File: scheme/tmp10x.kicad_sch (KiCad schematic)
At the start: 8 parts, among them U6 TMP100, U7 TMP100

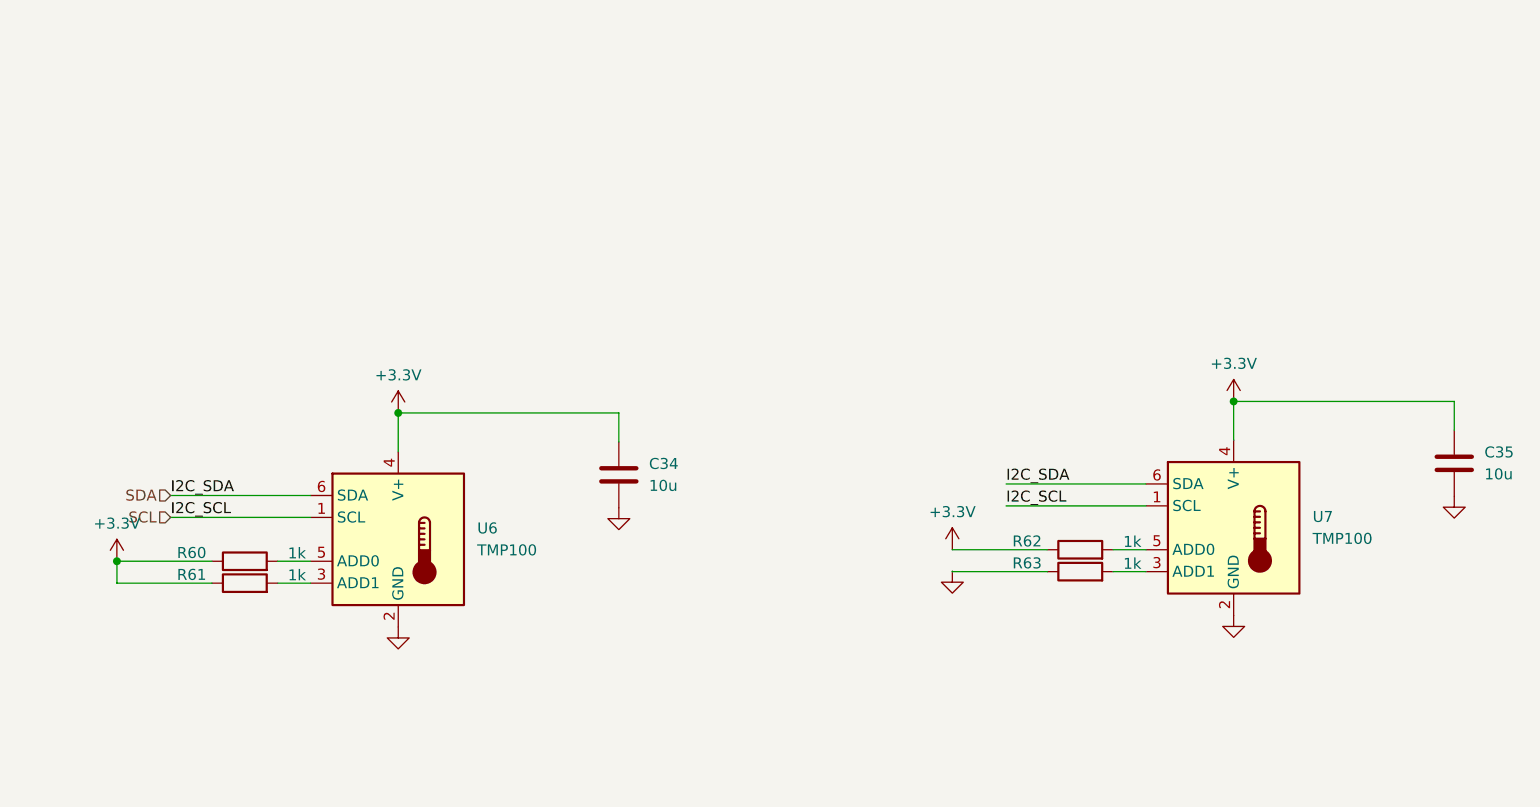
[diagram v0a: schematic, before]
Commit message: feat(schematic): fix peripheral sheets and integrate STM32G0B1CCT6
Главный МК заменён на STM32G0B1CCT6 (LQFP-48, pin-to-pin совместим
с STM32G071CBT6). Лист cpu переписан: обвязка по DS13560, LSE
32.768 кГц, подстроечник на ADC (PA4), перемычка JP_IDD, таблица
назначения выводов.

Исправлены листы периферии:
- st_link: перепутанные USB D+/D-, закороченные резисторы SWD,
  VBUS через PTC и Шоттки, ESD USBLC6-2SC6, LDO AP7361C-33E,
  SWO стянут на землю, J2 1x5 с NRST, перемычка JP_STL_PWR;
- ft232rl: 3V3OUT отвязан от общей шины +3.3V, разделены цепи
  TX/RX и светодиодов, ESD, Шоттки на VBUS, делитель на RESET#;
- w5500: номиналы терминации MDI (49.9 Ом / 10 Ом), PMODE=111,
  RSVD на GND, бусина аналогового питания, подтяжки RST/SCS/INT;
- w32: флэш W25Q32JVSSIQ, символ microSD с детектом карты,
  подтяжки линий SD;
- tmp10x: подтяжки I2C, адреса без резисторов, развязка 100 нФ.

Добавлен лист headers: разъёмы Arduino Uno R3 без ICSP, гребёнки
логического анализатора 1x27 с двух сторон, перемычки JP_SWD.
Удалён пустой лист memory. ERC: 0 ошибок.
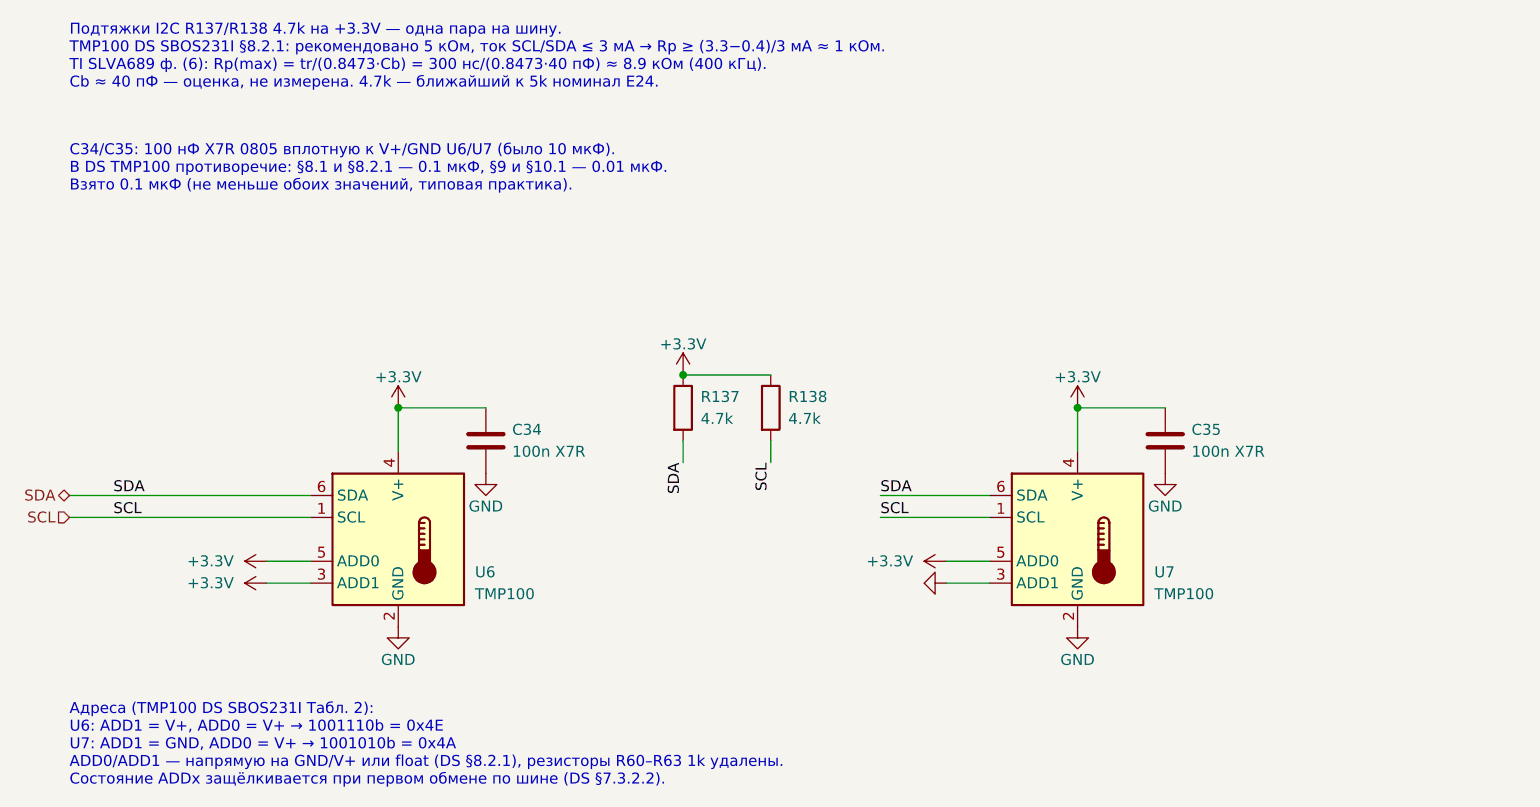
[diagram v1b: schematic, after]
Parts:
- removed R60, R61, R62, R63: 1k, symbol Device:R
- added R137, R138: 4.7k, Resistor_SMD:R_0805_2012Metric, symbol Device:R
- C34, C35: value 10u -> 100n X7R; footprint (none) -> Capacitor_SMD:C_0805_2012Metric
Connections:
- net +3.3V: now also U6.3 (ADD1), U6.5 (ADD0), U7.5 (ADD0), R137.1, R138.1
- net GND: now also U7.3 (ADD1)
- net SCL: now also R138.2
- net SDA: now also R137.2
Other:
- note added: "C34/C35: 100 нФ X7R 0805 вплотную к V+/GND U6/U7 (было 10 мкФ). В DS TMP100 противоречие: §8.1 и §8.2.1 — 0.1 мкФ, §9 и §10.1 — 0.01 мкФ. Взято 0.1 мкФ (не меньше обоих значений, типовая практика)."
- note added: "Адреса (TMP100 DS SBOS231I Табл. 2): U6: ADD1 = V+, ADD0 = V+ → 1001110b = 0x4E U7: ADD1 = GND, ADD0 = V+ → 1001010b = 0x4A ADD0/ADD1 — напрямую на GND/V+ или float (DS §8.2.1), резисторы R60–R63 1k удалены. Состояние ADDx защёлкивается при первом обмене по шине (DS §7.3.2.2)."
- note added: "Подтяжки I2C R137/R138 4.7k на +3.3V — одна пара на шину. TMP100 DS SBOS231I §8.2.1: рекомендовано 5 кОм, ток SCL/SDA ≤ 3 мА → Rp ≥ (3.3−0.4)/3 мА ≈ 1 кОм. TI SLVA689 ф. (6): Rp(max) = tr/(0.8473·Cb) = 300 нс/(0.8473·40 пФ) ≈ 8.9 кОм (400 кГц). Cb ≈ 40 пФ — оценка, не измерена. 4.7k — ближайший к 5k номинал E24."
- moved on the sheet: C34, C35, U7

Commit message: refactor(schematic): re-annotate references by sheet number
Позиционные обозначения перенумерованы по схеме «номер листа x 100»:
cpu - 1xx, st_link - 2xx, ft232rl - 3xx, w5500 - 4xx, w32 - 5xx,
tmp10x - 6xx, leds - 7xx, headers - 8xx. По обозначению на плате
сразу видно, к какому листу относится компонент.

Ссылки на компоненты в текстовых комментариях обновлены. Обозначения
из сторонних референсных схем (MB1136, MB1184, W5500-Ref, Ethernet
Shield, Adafruit) и имена выводов Arduino оставлены без изменений.

Проверено: нетлист до и после совпадает с точностью до переименования
(190 цепей, 187 компонентов), дубликатов нет, ERC - 0 ошибок.
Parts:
- renumbered C34 to C601, C35 to C602, R137 to R601, R138 to R602, U6 to U601, U7 to U602
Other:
- note added: "C601/C602: 100 нФ X7R 0805 вплотную к V+/GND U601/U602 (было 10 мкФ). В DS TMP100 противоречие: §8.1 и §8.2.1 — 0.1 мкФ, §9 и §10.1 — 0.01 мкФ. Взято 0.1 мкФ (не меньше обоих значений, типовая практика)."
- note added: "Адреса (TMP100 DS SBOS231I Табл. 2): U601: ADD1 = V+, ADD0 = V+ → 1001110b = 0x4E U602: ADD1 = GND, ADD0 = V+ → 1001010b = 0x4A ADD0/ADD1 — напрямую на GND/V+ или float (DS §8.2.1), резисторы R60–R63 1k удалены. Состояние ADDx защёлкивается при первом обмене по шине (DS §7.3.2.2)."
- note added: "Подтяжки I2C R601/R602 4.7k на +3.3V — одна пара на шину. TMP100 DS SBOS231I §8.2.1: рекомендовано 5 кОм, ток SCL/SDA ≤ 3 мА → Rp ≥ (3.3−0.4)/3 мА ≈ 1 кОм. TI SLVA689 ф. (6): Rp(max) = tr/(0.8473·Cb) = 300 нс/(0.8473·40 пФ) ≈ 8.9 кОм (400 кГц). Cb ≈ 40 пФ — оценка, не измерена. 4.7k — ближайший к 5k номинал E24."
- note removed: "C34/C35: 100 нФ X7R 0805 вплотную к V+/GND U6/U7 (было 10 мкФ). В DS TMP100 противоречие: §8.1 и §8.2.1 — 0.1 мкФ, §9 и §10.1 — 0.01 мкФ. Взято 0.1 мкФ (не меньше обоих значений, типовая практика)."
- note removed: "Адреса (TMP100 DS SBOS231I Табл. 2): U6: ADD1 = V+, ADD0 = V+ → 1001110b = 0x4E U7: ADD1 = GND, ADD0 = V+ → 1001010b = 0x4A ADD0/ADD1 — напрямую на GND/V+ или float (DS §8.2.1), резисторы R60–R63 1k удалены. Состояние ADDx защёлкивается при первом обмене по шине (DS §7.3.2.2)."
- note removed: "Подтяжки I2C R137/R138 4.7k на +3.3V — одна пара на шину. TMP100 DS SBOS231I §8.2.1: рекомендовано 5 кОм, ток SCL/SDA ≤ 3 мА → Rp ≥ (3.3−0.4)/3 мА ≈ 1 кОм. TI SLVA689 ф. (6): Rp(max) = tr/(0.8473·Cb) = 300 нс/(0.8473·40 пФ) ≈ 8.9 кОм (400 кГц). Cb ≈ 40 пФ — оценка, не измерена. 4.7k — ближайший к 5k номинал E24."
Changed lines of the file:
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@@
 	(generator_version "10.0")
 	(paper "A4")
-	(text "Подтяжки I2C R137/R138 4.7k на +3.3V — одна пара на шину.\nTMP100 DS SBOS231I §8.2.1: рекомендовано 5 кОм, ток SCL/SDA ≤ 3 мА → Rp ≥ (3.3−0.4)/3 мА ≈ 1 кОм.\nTI SLVA689 ф. (6): Rp(max) = tr/(0.8473·Cb) = 300 нс/(0.8473·40 пФ) ≈ 8.9 кОм (400 кГц).\nCb ≈ 40 пФ — оценка, не измерена. 4.7k — ближайший к 5k номинал E24."
+	(text "Подтяжки I2C R601/R602 4.7k на +3.3V — одна пара на шину.\nTMP100 DS SBOS231I §8.2.1: рекомендовано 5 кОм, ток SCL/SDA ≤ 3 мА → Rp ≥ (3.3−0.4)/3 мА ≈ 1 кОм.\nTI SLVA689 ф. (6): Rp(max) = tr/(0.8473·Cb) = 300 нс/(0.8473·40 пФ) ≈ 8.9 кОм (400 кГц).\nCb ≈ 40 пФ — оценка, не измерена. 4.7k — ближайший к 5k номинал E24."
 		(exclude_from_sim no)
 		(at 63.5 30.48 0)
@@
 		)
 	)
-	(text "Адреса (TMP100 DS SBOS231I Табл. 2):\nU6: ADD1 = V+, ADD0 = V+ → 1001110b = 0x4E\nU7: ADD1 = GND, ADD0 = V+ → 1001010b = 0x4A\nADD0/ADD1 — напрямую на GND/V+ или float (DS §8.2.1), резисторы R60–R63 1k удалены.\nСостояние ADDx защёлкивается при первом обмене по шине (DS §7.3.2.2)."
+	(text "Адреса (TMP100 DS SBOS231I Табл. 2):\nU601: ADD1 = V+, ADD0 = V+ → 1001110b = 0x4E\nU602: ADD1 = GND, ADD0 = V+ → 1001010b = 0x4A\nADD0/ADD1 — напрямую на GND/V+ или float (DS §8.2.1), резисторы R60–R63 1k удалены.\nСостояние ADDx защёлкивается при первом обмене по шине (DS §7.3.2.2)."
 		(exclude_from_sim no)
 		(at 63.5 109.22 0)
@@
 		)
 	)
-	(text "C34/C35: 100 нФ X7R 0805 вплотную к V+/GND U6/U7 (было 10 мкФ).\nВ DS TMP100 противоречие: §8.1 и §8.2.1 — 0.1 мкФ, §9 и §10.1 — 0.01 мкФ.\nВзято 0.1 мкФ (не меньше обоих значений, типовая практика)."
+	(text "C601/C602: 100 нФ X7R 0805 вплотную к V+/GND U601/U602 (было 10 мкФ).\nВ DS TMP100 противоречие: §8.1 и §8.2.1 — 0.1 мкФ, §9 и §10.1 — 0.01 мкФ.\nВзято 0.1 мкФ (не меньше обоих значений, типовая практика)."
 		(exclude_from_sim no)
 		(at 63.5 44.45 0)
@@
 		(in_pos_files yes)
 		(dnp no)
-		(property "Reference" "R137"
+		(property "Reference" "R601"
 			(at 136.652 73.66 0)
 			(show_name no)
@@
 			(project "g0_dev_board"
 				(path "/997acf0a-b54e-4c77-ad84-80f8d6e2dc27/1fdcf67e-4ae0-44bf-b3bf-1ed7985b8be2"
-					(reference "R137")
+					(reference "R601")
 					(unit 1)
 				)
@@
 		(in_pos_files yes)
 		(dnp no)
-		(property "Reference" "#PWR088"
+		(property "Reference" "#PWR0117"
 			(at 134.62 74.93 0)
 			(hide yes)
@@
 			(project "g0_dev_board"
 				(path "/997acf0a-b54e-4c77-ad84-80f8d6e2dc27/1fdcf67e-4ae0-44bf-b3bf-1ed7985b8be2"
-					(reference "#PWR088")
+					(reference "#PWR0117")
 					(unit 1)
 				)
@@
 		(in_pos_files yes)
 		(dnp no)
-		(property "Reference" "#PWR087"
+		(property "Reference" "#PWR0119"
 			(at 171.45 95.25 90)
 			(hide yes)
@@
 			(project "g0_dev_board"
 				(path "/997acf0a-b54e-4c77-ad84-80f8d6e2dc27/1fdcf67e-4ae0-44bf-b3bf-1ed7985b8be2"
-					(reference "#PWR087")
+					(reference "#PWR0119")
 					(unit 1)
 				)
@@
 		(in_pos_files yes)
 		(dnp no)
-		(property "Reference" "C35"
+		(property "Reference" "C602"
 			(at 193.548 77.47 0)
 			(show_name no)
@@
 			(project "g0_dev_board"
 				(path "/997acf0a-b54e-4c77-ad84-80f8d6e2dc27/1fdcf67e-4ae0-44bf-b3bf-1ed7985b8be2"
-					(reference "C35")
+					(reference "C602")
 					(unit 1)
 				)
@@
 		(in_pos_files yes)
 		(dnp no)
-		(property "Reference" "#PWR083"
+		(property "Reference" "#PWR0115"
 			(at 101.6 106.68 0)
 			(hide yes)
@@
 			(project "g0_dev_board"
 				(path "/997acf0a-b54e-4c77-ad84-80f8d6e2dc27/1fdcf67e-4ae0-44bf-b3bf-1ed7985b8be2"
-					(reference "#PWR083")
+					(reference "#PWR0115")
 					(unit 1)
 				)
@@
 		(in_pos_files yes)
 		(dnp no)
-		(property "Reference" "U7"
+		(property "Reference" "U602"
 			(at 189.23 93.98 0)
 			(show_name no)
@@
 			(project "g0_dev_board"
 				(path "/997acf0a-b54e-4c77-ad84-80f8d6e2dc27/1fdcf67e-4ae0-44bf-b3bf-1ed7985b8be2"
-					(reference "U7")
+					(reference "U602")
 					(unit 1)
 				)
@@
 		(in_pos_files yes)
 		(dnp no)
-		(property "Reference" "#PWR1305"
+		(property "Reference" "#PWR0118"
 			(at 168.91 92.71 90)
 			(hide yes)
@@
 			(project "g0_dev_board"
 				(path "/997acf0a-b54e-4c77-ad84-80f8d6e2dc27/1fdcf67e-4ae0-44bf-b3bf-1ed7985b8be2"
-					(reference "#PWR1305")
+					(reference "#PWR0118")
 					(unit 1)
 				)
@@
 		(in_pos_files yes)
 		(dnp no)
-		(property "Reference" "U6"
+		(property "Reference" "U601"
 			(at 110.49 93.98 0)
 			(show_name no)
@@
 			(project "g0_dev_board"
 				(path "/997acf0a-b54e-4c77-ad84-80f8d6e2dc27/1fdcf67e-4ae0-44bf-b3bf-1ed7985b8be2"
-					(reference "U6")
+					(reference "U601")
 					(unit 1)
 				)
@@
 		(in_pos_files yes)
 		(dnp no)
-		(property "Reference" "C34"
+		(property "Reference" "C601"
 			(at 114.808 77.47 0)
 			(show_name no)
@@
 			(project "g0_dev_board"
 				(path "/997acf0a-b54e-4c77-ad84-80f8d6e2dc27/1fdcf67e-4ae0-44bf-b3bf-1ed7985b8be2"
-					(reference "C34")
+					(reference "C601")
 					(unit 1)
 				)
@@
 		(in_pos_files yes)
 		(dnp no)
-		(property "Reference" "#PWR1306"
+		(property "Reference" "#PWR0120"
 			(at 180.34 78.74 0)
 			(hide yes)
@@
 			(project "g0_dev_board"
 				(path "/997acf0a-b54e-4c77-ad84-80f8d6e2dc27/1fdcf67e-4ae0-44bf-b3bf-1ed7985b8be2"
-					(reference "#PWR1306")
+					(reference "#PWR0120")
 					(unit 1)
 				)
@@
 		(in_pos_files yes)
 		(dnp no)
-		(property "Reference" "#PWR085"
+		(property "Reference" "#PWR0113"
 			(at 90.17 95.25 90)
 			(hide yes)
@@
 			(project "g0_dev_board"
 				(path "/997acf0a-b54e-4c77-ad84-80f8d6e2dc27/1fdcf67e-4ae0-44bf-b3bf-1ed7985b8be2"
-					(reference "#PWR085")
+					(reference "#PWR0113")
 					(unit 1)
 				)
@@
 		(in_pos_files yes)
 		(dnp no)
-		(property "Reference" "#PWR086"
+		(property "Reference" "#PWR0114"
 			(at 101.6 78.74 0)
 			(hide yes)
@@
 			(project "g0_dev_board"
 				(path "/997acf0a-b54e-4c77-ad84-80f8d6e2dc27/1fdcf67e-4ae0-44bf-b3bf-1ed7985b8be2"
-					(reference "#PWR086")
+					(reference "#PWR0114")
 					(unit 1)
 				)
@@
 		(in_pos_files yes)
 		(dnp no)
-		(property "Reference" "#PWR084"
+		(property "Reference" "#PWR0112"
 			(at 90.17 92.71 90)
 			(hide yes)
@@
 			(project "g0_dev_board"
 				(path "/997acf0a-b54e-4c77-ad84-80f8d6e2dc27/1fdcf67e-4ae0-44bf-b3bf-1ed7985b8be2"
-					(reference "#PWR084")
+					(reference "#PWR0112")
 					(unit 1)
 				)
@@
 		(in_pos_files yes)
 		(dnp no)
-		(property "Reference" "R138"
+		(property "Reference" "R602"
 			(at 146.812 73.66 0)
 			(show_name no)
@@
 			(project "g0_dev_board"
 				(path "/997acf0a-b54e-4c77-ad84-80f8d6e2dc27/1fdcf67e-4ae0-44bf-b3bf-1ed7985b8be2"
-					(reference "R138")
+					(reference "R602")
 					(unit 1)
 				)
@@
 		(in_pos_files yes)
 		(dnp no)
-		(property "Reference" "#PWR082"
+		(property "Reference" "#PWR0116"
 			(at 111.76 88.9 0)
 			(hide yes)
@@
 			(project "g0_dev_board"
 				(path "/997acf0a-b54e-4c77-ad84-80f8d6e2dc27/1fdcf67e-4ae0-44bf-b3bf-1ed7985b8be2"
-					(reference "#PWR082")
+					(reference "#PWR0116")
 					(unit 1)
 				)
@@
 		(in_pos_files yes)
 		(dnp no)
-		(property "Reference" "#PWR090"
+		(property "Reference" "#PWR0121"
 			(at 180.34 106.68 0)
 			(hide yes)
@@
 			(project "g0_dev_board"
 				(path "/997acf0a-b54e-4c77-ad84-80f8d6e2dc27/1fdcf67e-4ae0-44bf-b3bf-1ed7985b8be2"
-					(reference "#PWR090")
+					(reference "#PWR0121")
 					(unit 1)
 				)
@@
 		(in_pos_files yes)
 		(dnp no)
-		(property "Reference" "#PWR089"
+		(property "Reference" "#PWR0122"
 			(at 190.5 88.9 0)
 			(hide yes)
@@
 			(project "g0_dev_board"
 				(path "/997acf0a-b54e-4c77-ad84-80f8d6e2dc27/1fdcf67e-4ae0-44bf-b3bf-1ed7985b8be2"
-					(reference "#PWR089")
-					(unit 1)
-				)
+					(reference "#PWR0122")
+					(unit 1)
+				)

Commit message: feat(schematic): add MPN/LCSC fields and fix Q201 pinout
Подготовка к заказу сборки на JLCPCB:
- всем монтируемым символам добавлено скрытое поле LCSC (коды
  проверены через API JLCPCB, по возможности Basic);
- LSE Y101: Epson FC-135 CL 7 пФ (Q13FC13500002), C106/C108 6.8p C0G,
  footprint под ручную пайку; в SDK нужен LSEDRV=10;
- бусины: FB101/FB401 GZ2012D601TF, FB301 BLM21PG221SN1D (2 А);
- Y401 25 МГц X49SD25MSD2SC (CL 20 пФ), C401/C402 27p -> 33p;
- Y201 8 МГц X49SD8MSD2SC, нагрузочные 22p оставлены (предел F103
  25 пФ, сдвиг частоты для USB FS несущественен);
- C505 100n на ~CARD_DET (антидребезг), ссылка на чертёж Hirose.

Исправления:
- Q201: символ SS9013 с распиновкой TO-92 (1=E 2=B 3=C) стоял на
  footprint SOT-23 (1=B 2=E 3=C) - транзистор встал бы неправильно.
  Заменён на MMBT3904 (SOT-23, Basic), цепи B/E/C сохранены;
- лист leds переведён с 1206 на 0805, R701/R702 630 -> 680 Ом
  (630 нет в E24), LD702 ORANGE -> RED;
- C301 (DNP) получил номинал 4.7n, опечатка 25Mhz в Y401.

ERC: 0 ошибок, 0 предупреждений.
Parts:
- C601, C602: LCSC (none) -> C49678
- R601, R602: LCSC (none) -> C17673
- U601, U602: LCSC (none) -> C31810
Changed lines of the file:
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@@
+			)
+		)
+		(property "LCSC" "C17673"
+			(at 134.62 74.93 0)
+			(hide yes)
+			(show_name no)
+			(do_not_autoplace no)
+			(effects
+				(font
+					(size 1.27 1.27)
+				)
 			)
 		)
@@
 			)
 		)
+		(property "LCSC" "C49678"
+			(at 190.5 78.74 0)
+			(hide yes)
+			(show_name no)
+			(do_not_autoplace no)
+			(effects
+				(font
+					(size 1.27 1.27)
+				)
+			)
+		)
 		(pin "2"
 		)
@@
 			)
 		)
+		(property "LCSC" "C31810"
+			(at 180.34 90.17 0)
+			(hide yes)
+			(show_name no)
+			(do_not_autoplace no)
+			(effects
+				(font
+					(size 1.27 1.27)
+				)
+			)
+		)
 		(pin "6"
 		)
@@
 			)
 		)
+		(property "LCSC" "C31810"
+			(at 101.6 90.17 0)
+			(hide yes)
+			(show_name no)
+			(do_not_autoplace no)
+			(effects
+				(font
+					(size 1.27 1.27)
+				)
+			)
+		)
 		(pin "6"
 		)
@@
 			)
 		)
+		(property "LCSC" "C49678"
+			(at 111.76 78.74 0)
+			(hide yes)
+			(show_name no)
+			(do_not_autoplace no)
+			(effects
+				(font
+					(size 1.27 1.27)
+				)
+			)
+		)
 		(pin "2"
 		)
@@
 			(at 144.78 74.93 0)
 			(hide yes)
+			(show_name no)
+			(do_not_autoplace no)
+			(effects
+				(font
+					(size 1.27 1.27)
+				)
+			)
+		)
+		(property "LCSC" "C17673"
+			(at 144.78 74.93 0)
+			(hide yes)
